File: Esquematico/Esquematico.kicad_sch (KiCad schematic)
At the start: 9 parts, among them SW1 Pulsador, U1 ATmega328P-P, U2 L7805, Y1 16Mhz

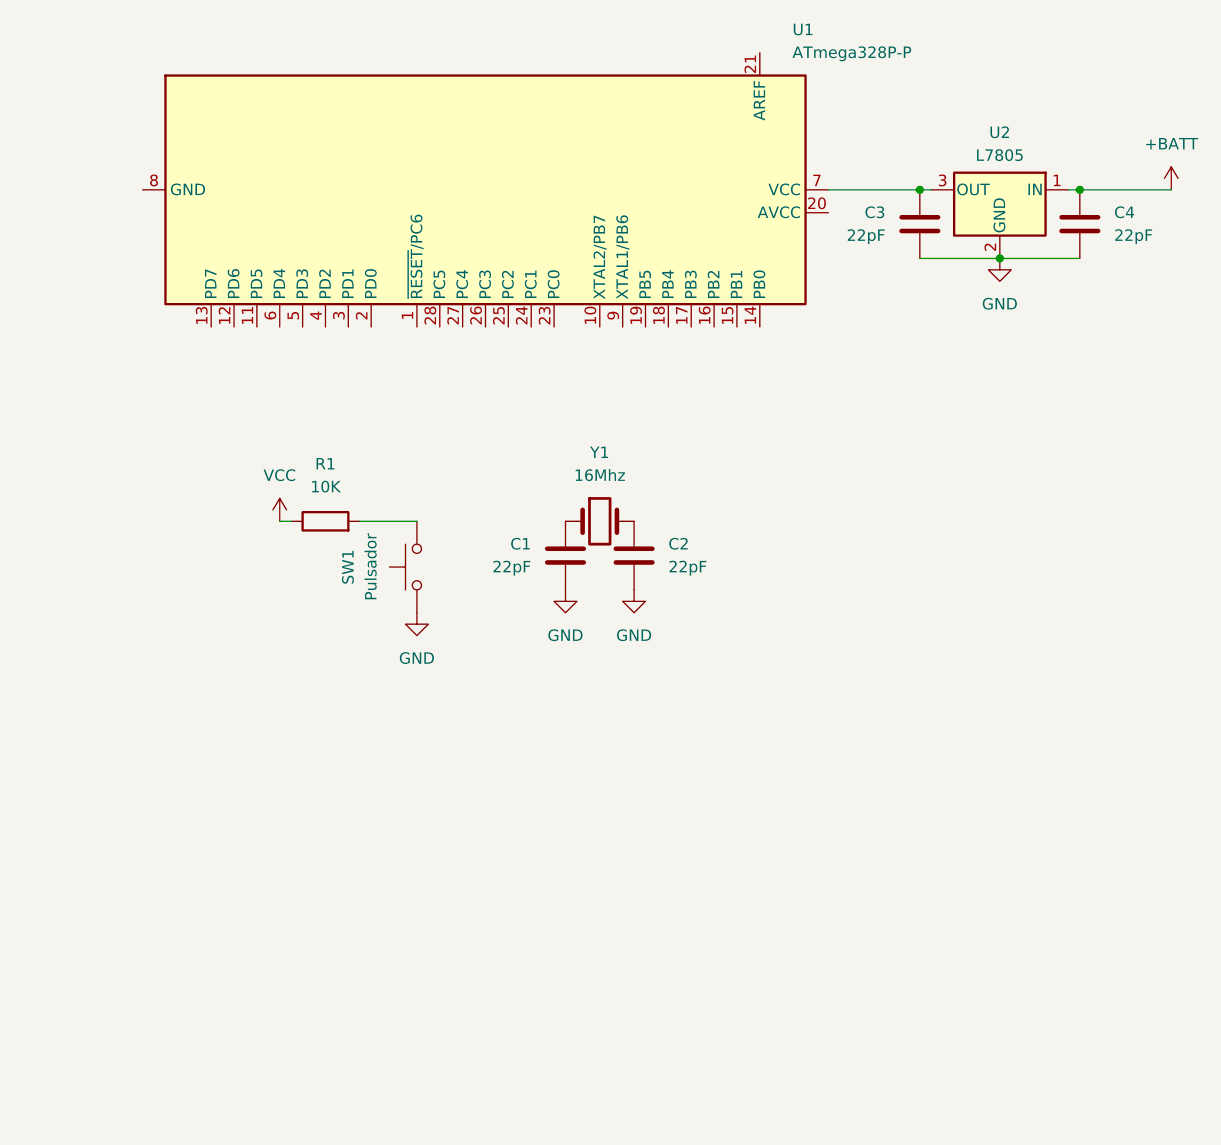
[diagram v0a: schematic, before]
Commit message: Codigo funcionando sin reversa y con timer 0 conectado
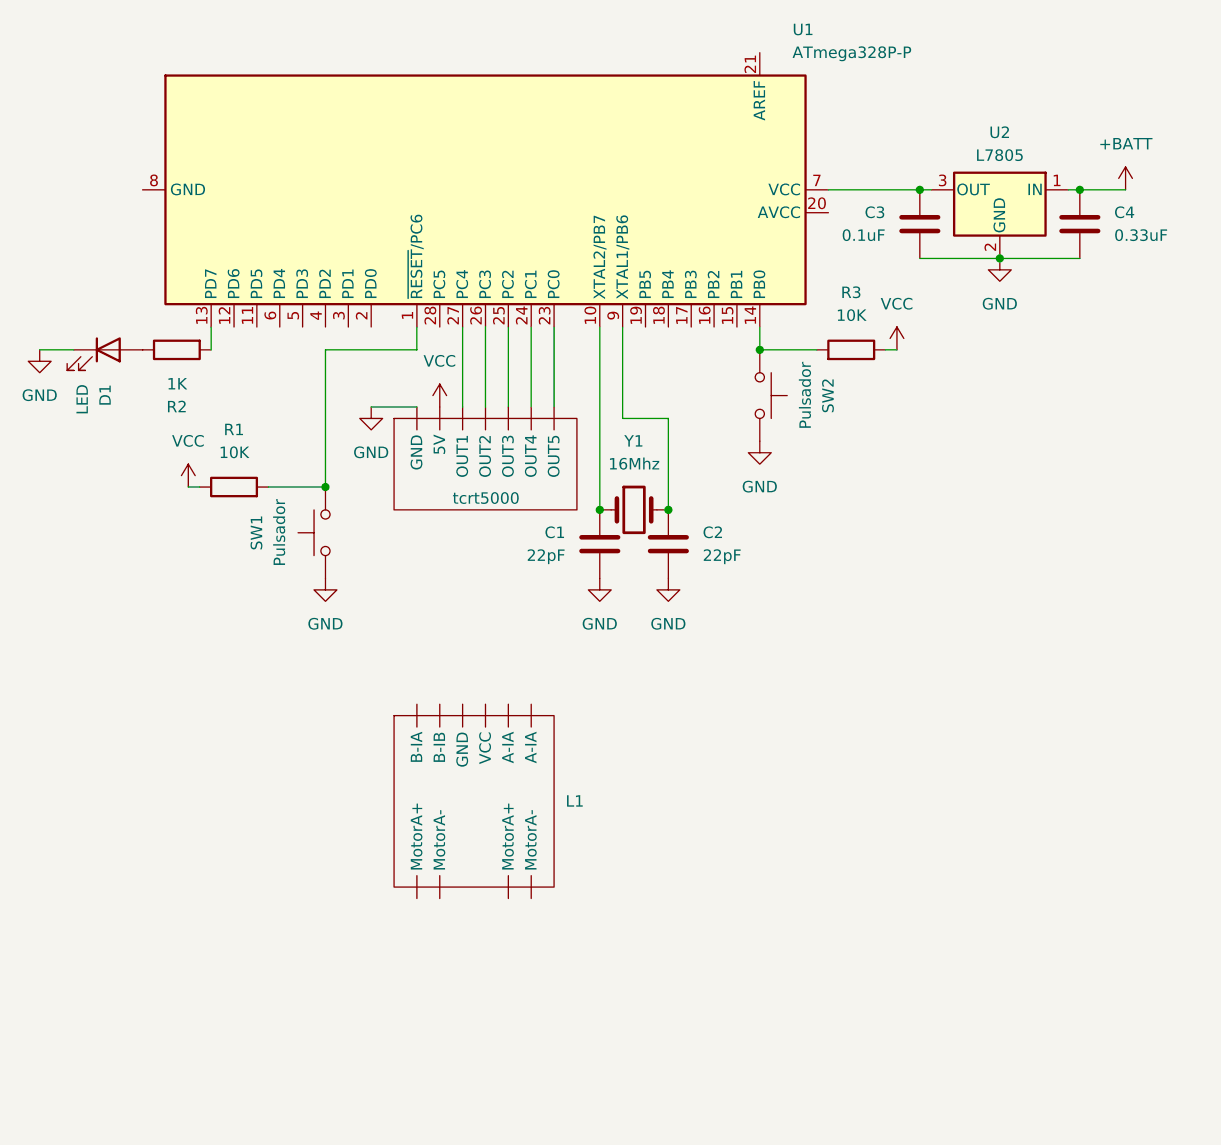
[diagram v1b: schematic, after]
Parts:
- added D1: LED, symbol Device:LED
- added L1: ~, symbol L9110:L9110
- added R2: 1K, symbol Device:R
- added R3: 10K, symbol Device:R
- added SW2: Pulsador, symbol Switch:SW_Push
- added tcrt5000: ~, symbol tcrt5000:tcrt5000
- C3: value 22pF -> 0.1uF
- C4: value 22pF -> 0.33uF
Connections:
- net GND: now also D1.1 (K), SW2.1, tcrt5000. (OUT5)
- net VCC: now also R3.1, tcrt5000. (OUT5)
- net at C1.1, Y1.1: now also U1.10 (XTAL2/PB7)
- net at C2.1, Y1.2: now also U1.9 (XTAL1/PB6)
- net at R1.2, SW1.2: now also U1.1 (~{RESET}/PC6)
- net at U1.13 (PD7): now also R2.2
- net at U1.14 (PB0): now also R3.2, SW2.2
- net at U1.23 (PC0): now also tcrt5000. (OUT5)
- net at U1.24 (PC1): now also tcrt5000. (OUT5)
- net at U1.25 (PC2): now also tcrt5000. (OUT5)
- net at U1.26 (PC3): now also tcrt5000. (OUT5)
- net at U1.27 (PC4): now also tcrt5000. (OUT5)
- new net: D1.2 (A), R2.1
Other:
- moved on the sheet: C1, C2, R1, SW1, Y1

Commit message: Termino el esquemático
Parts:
- removed L1: ~, symbol L9110:L9110
- added L9110: ~, symbol L9110:L9110
- added M1, M2: Motor_DC, symbol Motor:Motor_DC
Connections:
- net at U1.11 (PD5): now also L9110. (VCC)
- net at U1.12 (PD6): now also L9110. (VCC)
- net at U1.15 (PB1): now also L9110. (VCC)
- net at U1.16 (PB2): now also L9110. (VCC)
- new net: L9110. (VCC), M1.1 (+)
- new net: L9110. (VCC), M1.2 (-)
- new net: L9110. (VCC), M2.1 (+)
- new net: L9110. (VCC), M2.2 (-)
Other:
- moved on the sheet: R1, R3, SW1, SW2
